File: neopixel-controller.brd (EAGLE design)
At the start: 23.8 x 26.7 mm, 12 parts, among them J1 Power, U1 ATTiny85

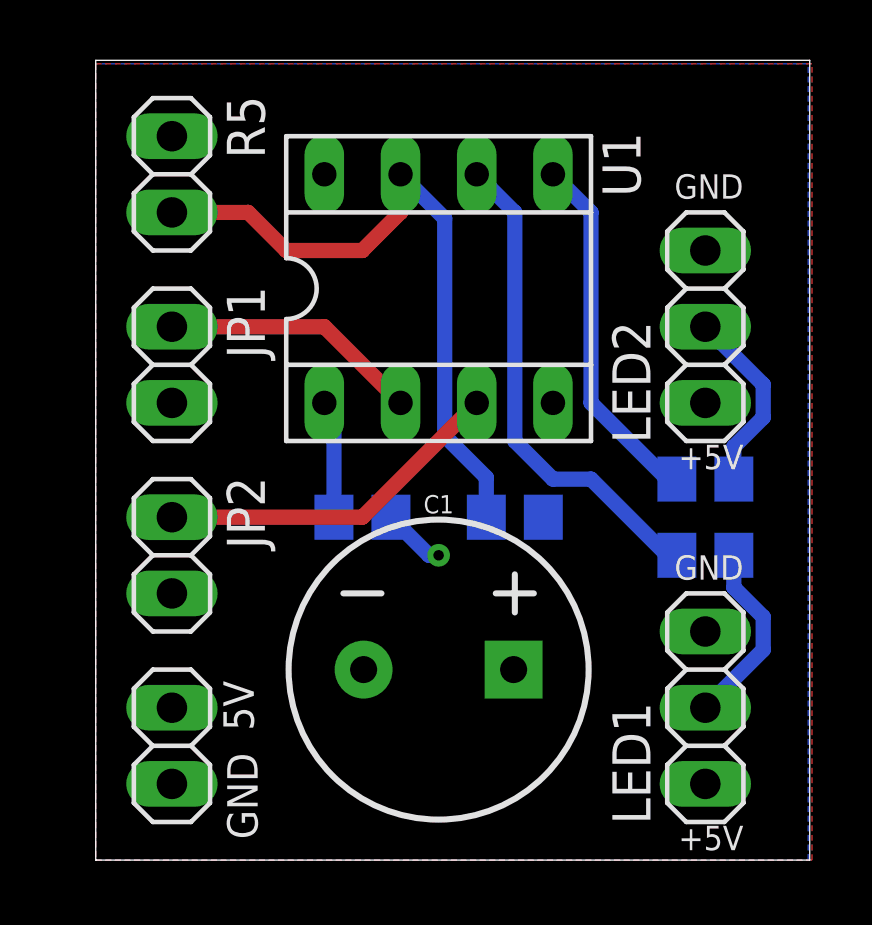
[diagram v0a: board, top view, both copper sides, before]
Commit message: Switch to both planes being ground planes
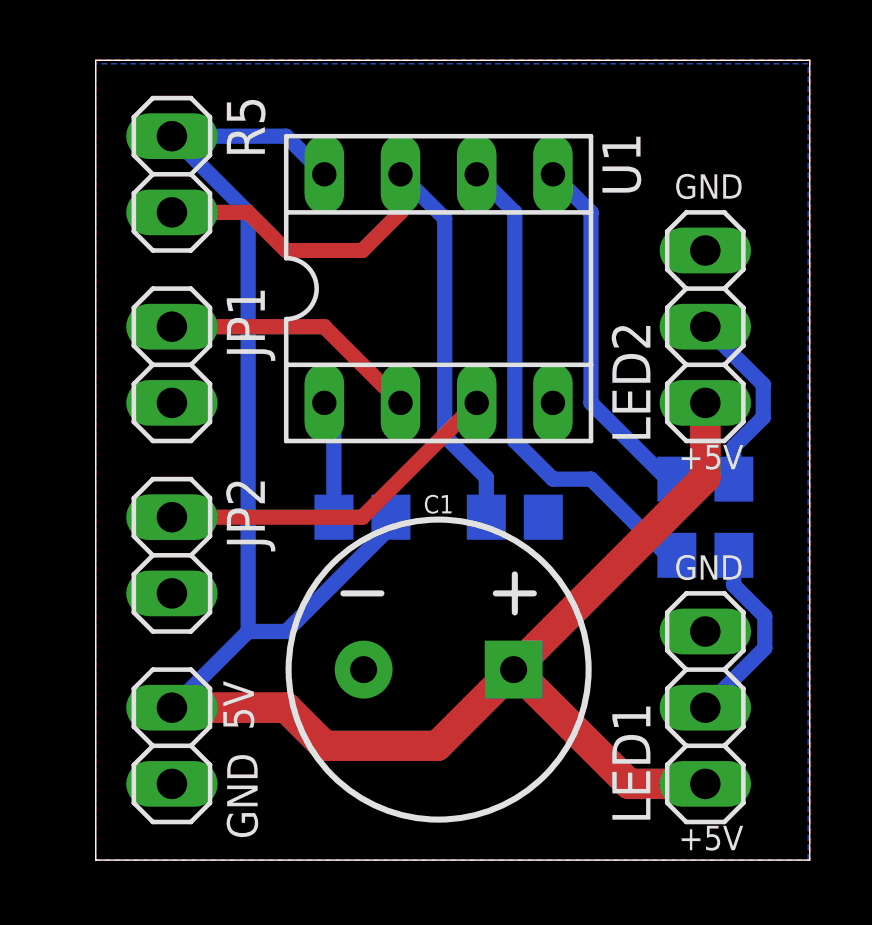
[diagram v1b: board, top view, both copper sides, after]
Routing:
- net VCC: track 2.12 -> 65.9 mm, vias 1 -> 0
- added copper zone on layer 1, net GND
- removed copper zone on layer 1, net VCC
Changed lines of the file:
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@@
 <?xml version="1.0" encoding="utf-8"?>
 <!DOCTYPE eagle SYSTEM "eagle.dtd">
-<eagle version="9.1.0">
+<eagle version="9.2.2">
 <drawing>
 <settings>
-<setting alwaysvectorfont="no"/>
+<setting alwaysvectorfont="yes"/>
 <setting verticaltext="up"/>
 </settings>
@@
 <classes>
 <class number="0" name="default" width="0" drill="0">
+<clearance class="0" value="0.205"/>
 </class>
 </classes>
@@
 </autorouter>
 <elements>
-<element name="C1" library="SparkFun-Capacitors" package="CPOL-RADIAL-5MM-10MM" value="1mF" x="11.43" y="6.35">
+<element name="C1" library="SparkFun-Capacitors" package="CPOL-RADIAL-5MM-10MM" value="1mF" x="11.43" y="6.35" smashed="yes">
+<attribute name="NAME" x="11.43" y="11.557" size="0.6096" layer="25" font="vector" ratio="20" align="bottom-center"/>
 <attribute name="PROD_ID" value="CAP-09538" x="11.43" y="6.35" size="1.778" layer="27" display="off"/>
+<attribute name="VALUE" x="11.43" y="1.143" size="0.6096" layer="27" font="vector" ratio="20" align="top-center"/>
 </element>
 <element name="J1" library="pinhead" library_urn="urn:adsk.eagle:library:325" package="1X02" package3d_urn="urn:adsk.eagle:package:22435/2" value="Power" x="2.54" y="3.81" smashed="yes" rot="R270">
@@
 <attribute name="VALUE" x="8.382" y="18.542" size="1.27" layer="27" ratio="10"/>
 </element>
-<element name="LED1" library="JoshCustom" package="NEOPIXEL_PINHEAD" value="Neopixel" x="20.32" y="5.08" rot="R90"/>
-<element name="LED2" library="JoshCustom" package="NEOPIXEL_PINHEAD" value="Neopixel" x="20.32" y="17.78" rot="R90"/>
+<element name="LED1" library="JoshCustom" package="NEOPIXEL_PINHEAD" value="Neopixel" x="20.32" y="5.08" smashed="yes" rot="R90">
+<attribute name="NAME" x="18.4912" y="1.1938" size="1.27" layer="25" font="vector" rot="R90"/>
+<attribute name="VALUE" x="23.495" y="1.27" size="1.27" layer="27" font="vector" rot="R90"/>
+</element>
+<element name="LED2" library="JoshCustom" package="NEOPIXEL_PINHEAD" value="Neopixel" x="20.32" y="17.78" smashed="yes" rot="R90">
+<attribute name="NAME" x="18.4912" y="13.8938" size="1.27" layer="25" font="vector" rot="R90"/>
+<attribute name="VALUE" x="23.495" y="13.97" size="1.27" layer="27" font="vector" rot="R90"/>
+</element>
 </elements>
 <signals>
@@
 <contactref element="R4" pad="2"/>
 <contactref element="R5" pad="1"/>
-<polygon width="0.1524" layer="1" thermals="no">
-<vertex x="0" y="0"/>
-<vertex x="23.876" y="0"/>
-<vertex x="23.876" y="26.543"/>
-<vertex x="0" y="26.543"/>
-</polygon>
-<wire x1="9.84" y1="11.43" x2="11.11" y2="10.16" width="0.508" layer="16"/>
-<wire x1="11.11" y1="10.16" x2="11.43" y2="10.16" width="0.508" layer="16"/>
-<via x="11.43" y="10.16" extent="1-16" drill="0.35"/>
+<wire x1="2.54" y1="24.13" x2="5.08" y2="21.59" width="0.508" layer="16"/>
+<wire x1="5.08" y1="21.59" x2="5.08" y2="7.62" width="0.508" layer="16"/>
+<wire x1="5.08" y1="7.62" x2="2.54" y2="5.08" width="0.508" layer="16"/>
+<wire x1="2.54" y1="24.13" x2="6.35" y2="24.13" width="0.508" layer="16"/>
+<wire x1="6.35" y1="24.13" x2="7.62" y2="22.86" width="0.508" layer="16"/>
+<wire x1="5.08" y1="7.62" x2="6.35" y2="7.62" width="0.508" layer="16"/>
+<wire x1="6.35" y1="7.62" x2="10.16" y2="11.43" width="0.508" layer="16"/>
+<wire x1="2.54" y1="5.08" x2="6.35" y2="5.08" width="1.016" layer="1"/>
+<wire x1="6.35" y1="5.08" x2="7.62" y2="3.81" width="1.016" layer="1"/>
+<wire x1="7.62" y1="3.81" x2="11.39" y2="3.81" width="1.016" layer="1"/>
+<wire x1="11.39" y1="3.81" x2="13.93" y2="6.35" width="1.016" layer="1"/>
+<wire x1="13.93" y1="6.35" x2="20.32" y2="12.74" width="1.016" layer="1"/>
+<wire x1="20.32" y1="12.74" x2="20.32" y2="15.24" width="1.016" layer="1"/>
+<wire x1="13.93" y1="6.35" x2="13.97" y2="6.35" width="1.016" layer="1"/>
+<wire x1="17.78" y1="2.54" x2="20.32" y2="2.54" width="1.016" layer="1"/>
+<wire x1="13.97" y1="6.35" x2="17.78" y2="2.54" width="1.016" layer="1"/>
+<wire x1="10.16" y1="11.43" x2="9.84" y2="11.43" width="0" layer="19" extent="16-16"/>
 </signal>
 <signal name="GND">
@@
 <vertex x="0" y="26.543"/>
 </polygon>
+<polygon width="0.3048" layer="1">
+<vertex x="0" y="0"/>
+<vertex x="0" y="26.67"/>
+<vertex x="23.8125" y="26.67"/>
+<vertex x="23.8125" y="0"/>
+</polygon>
 </signal>
 <signal name="N$5">
@@
 <contactref element="LED1" pad="2"/>
 <contactref element="R2" pad="2"/>
-<wire x1="21.27" y1="9.08436875" x2="21.27" y2="10.16" width="0.508" layer="16"/>
-<wire x1="22.2504" y1="8.10396875" x2="21.27" y2="9.08436875" width="0.508" layer="16"/>
-<wire x1="22.2504" y1="7.0104" x2="22.2504" y2="8.10396875" width="0.508" layer="16"/>
-<wire x1="20.32" y1="5.08" x2="22.2504" y2="7.0104" width="0.508" layer="16"/>
+<wire x1="21.27" y1="9.15875625" x2="21.27" y2="10.16" width="0.508" layer="16"/>
+<wire x1="22.303" y1="8.12575625" x2="21.27" y2="9.15875625" width="0.508" layer="16"/>
+<wire x1="22.303" y1="7.063" x2="22.303" y2="8.12575625" width="0.508" layer="16"/>
+<wire x1="20.32" y1="5.08" x2="22.303" y2="7.063" width="0.508" layer="16"/>
 </signal>
 <signal name="PB3">
@@
 </note>
 <note version="8.3" severity="warning">
+Since Version 8.3, EAGLE supports Fusion synchronisation.
+This feature will not be available in this version and saving
+the document will break the link to the Fusion PCB feature.
+</note>
+<note version="8.3" severity="warning">

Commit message: Final revision
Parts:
- added C2: 0.1uF, resistor:C0805
- C1: value 1mF -> 1000uF; device SparkFun-Capacitors:CPOL-RADIAL-5MM-10MM -> JoshCustom:CAP-3,5-8
- moved C1 1.62 mm to (11.7, 4.76)
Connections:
- net GND: now also C1.NEGATIVE, C2.2; no longer C1.-
- net VCC: now also C1.POSITIVE, C2.1; no longer C1.+
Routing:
- net VCC: track 65.9 -> 73.6 mm

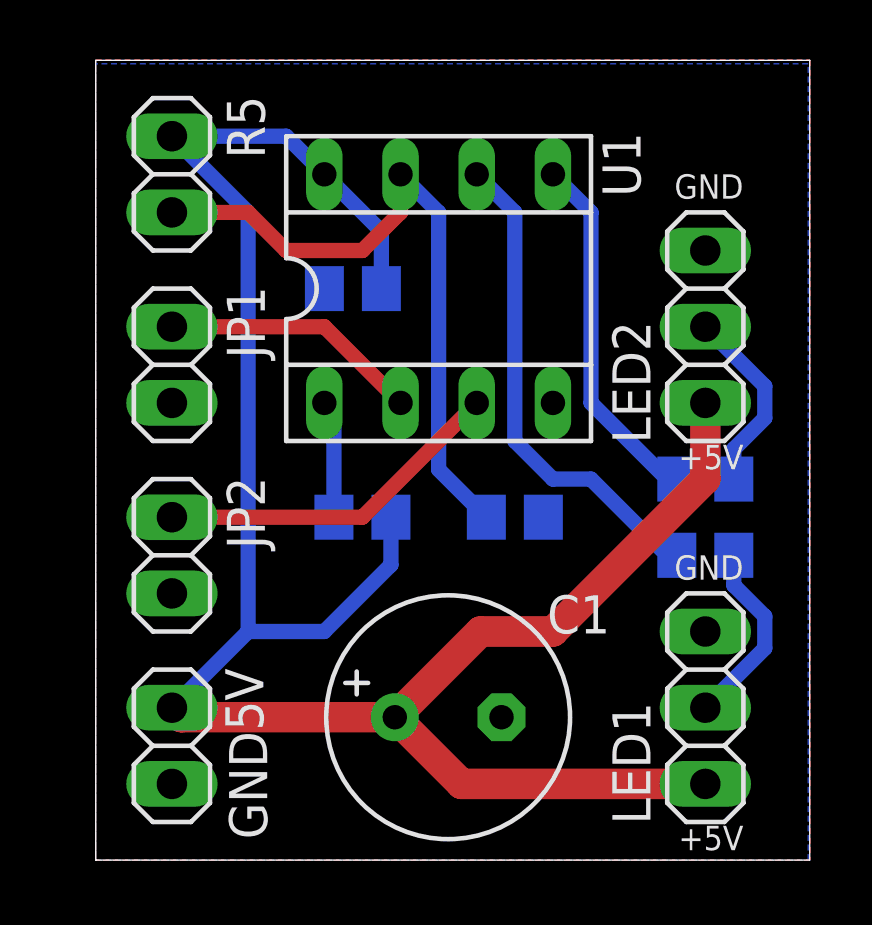
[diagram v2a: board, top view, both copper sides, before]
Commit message: Initial swap of Neopixel controller to SOIC ATTiny85
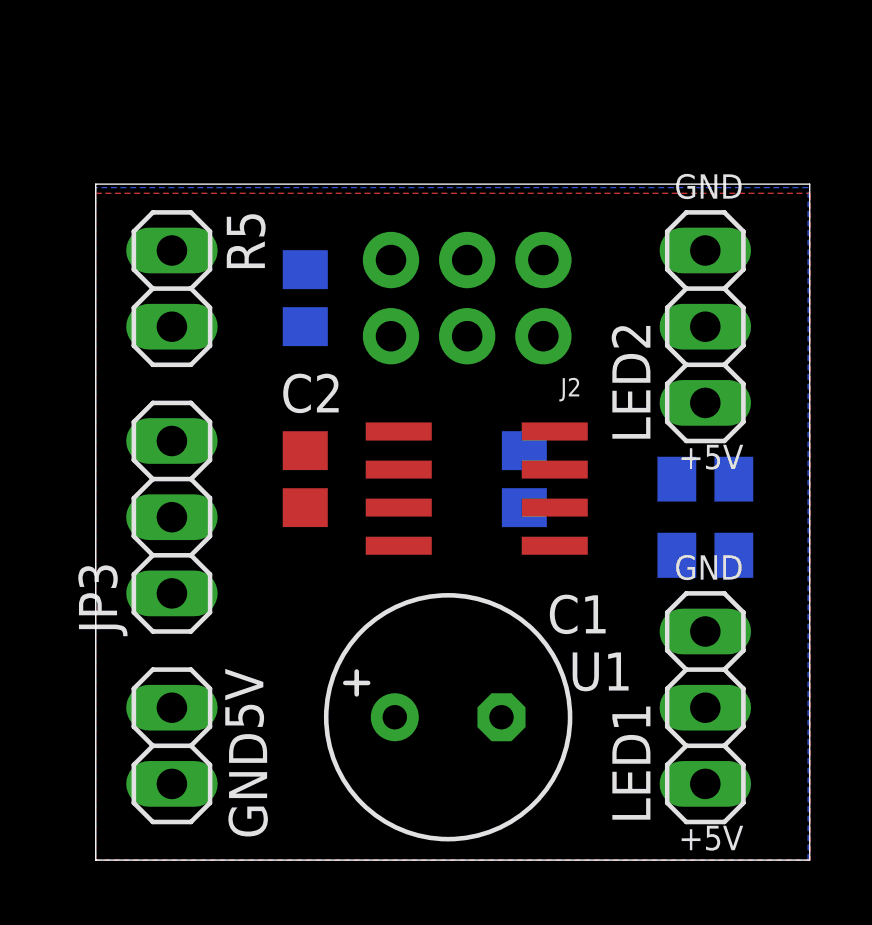
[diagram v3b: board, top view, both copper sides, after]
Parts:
- removed JP1, JP2: (no value), pinhead:1X02
- added J2: AVR_SPI_PROG_3X2NS, SparkFun-Connectors:2X3-NS
- added JP3: (no value), pinhead:1X03
- U1: device JoshCustom:SOCKET-08 -> JoshCustom:SOIC8
- moved R1 10.1 mm to (6.99, 18.7), turned to 90 degrees
- moved U1 6.79 mm to (12.7, 12.4), turned to 270 degrees
- moved C2 6.55 mm to (6.99, 12.7), flipped to the top, turned to 270 degrees
- moved R4 5.54 mm to (14.3, 12.7), turned to 270 degrees
- moved R5 3.81 mm to (2.54, 19.1)
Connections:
- removed net N$5: R4.1, U1.1
- new net RESET: J2.5, R4.1, U1.1
- net GND: now also J2.6, JP3.2; no longer JP1.2, JP2.2
- net LED1: now also J2.1
- net LED2: now also J2.4
- net PB2: now also J2.3
- net PB3: now also JP3.3; no longer JP1.1
- net PB4: now also JP3.1; no longer JP2.1
- net VCC: now also J2.2
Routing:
- net VCC: track 73.6 -> 0.00 mm
- net PB2: track 22.6 -> 0.00 mm
- net LED1: track 16.7 -> 0.00 mm
- net LED2: track 12.1 -> 0.00 mm
- net PB4: track 11.7 -> 0.00 mm
- net PB3: track 8.67 -> 0.00 mm
- net N$1: track 6.33 -> 0.00 mm
- net N$2: track 6.33 -> 0.00 mm
- net N$5: track 3.94 -> 0.00 mm
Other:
- board size 23.8 x 26.7 mm -> 23.8 x 22.5 mm

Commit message: Initial redesign for production run 2
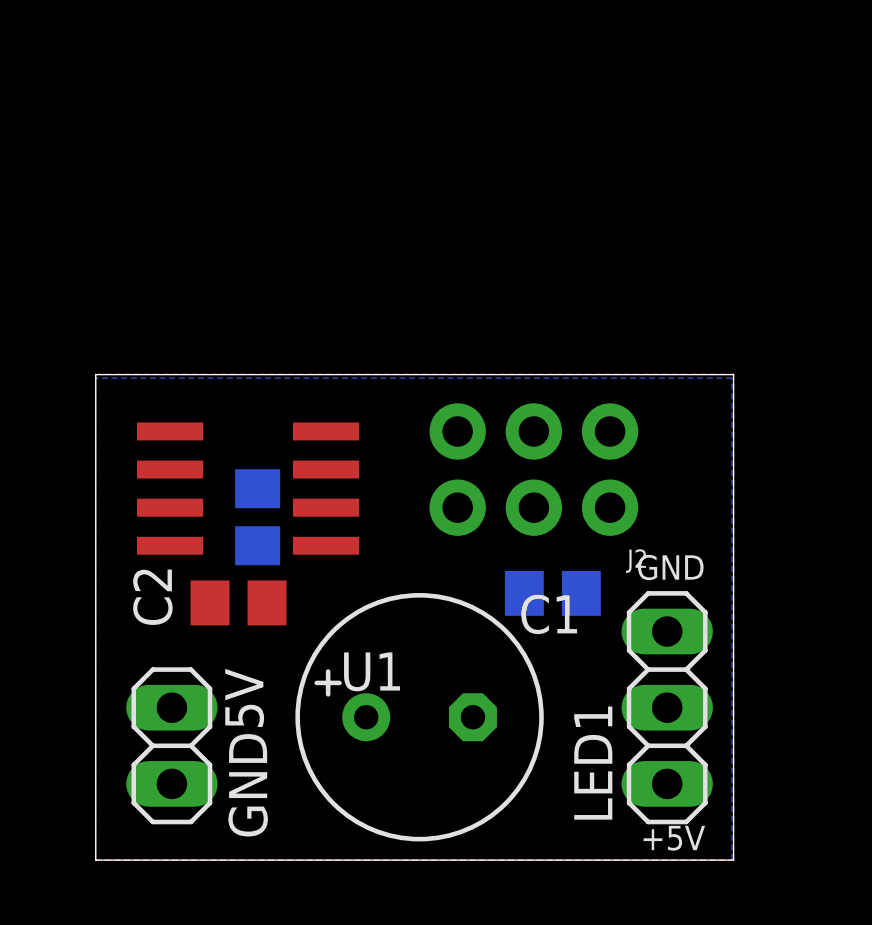
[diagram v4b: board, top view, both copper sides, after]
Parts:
- removed JP3: (no value), pinhead:1X03
- removed LED2: Neopixel, JoshCustom:NEOPIXEL_PINHEAD
- removed R1: 10k, resistor:R0805
- removed R3: 470, resistor:R0805
- removed R5: (no value), pinhead:1X02
- moved R4 8.98 mm to (5.40, 11.4)
- moved U1 7.62 mm to (5.08, 12.4)
- moved J2 6.13 mm to (14.6, 13.0)
- moved R2 5.24 mm to (15.2, 8.89)
- moved C2 4.69 mm to (4.76, 8.57), turned to 0 degrees
- moved LED1 1.27 mm to (19.1, 5.08)
- moved C1 0.95 mm to (10.8, 4.76)
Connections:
- removed net N$1: LED2.2, R3.2
- net GND: no longer JP3.2, LED2.3, R1.1
- net LED2: no longer R3.1
- net PB2: no longer R1.2, R5.2
- net PB3: no longer JP3.3
- net PB4: no longer JP3.1
- net VCC: no longer LED2.1, R5.1
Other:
- board size 23.8 x 22.5 mm -> 21.3 x 16.2 mm

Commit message: Revert neopixel-controller to neopixel-v1.0 and remove unnecessary things for 20th anniversary trophy production
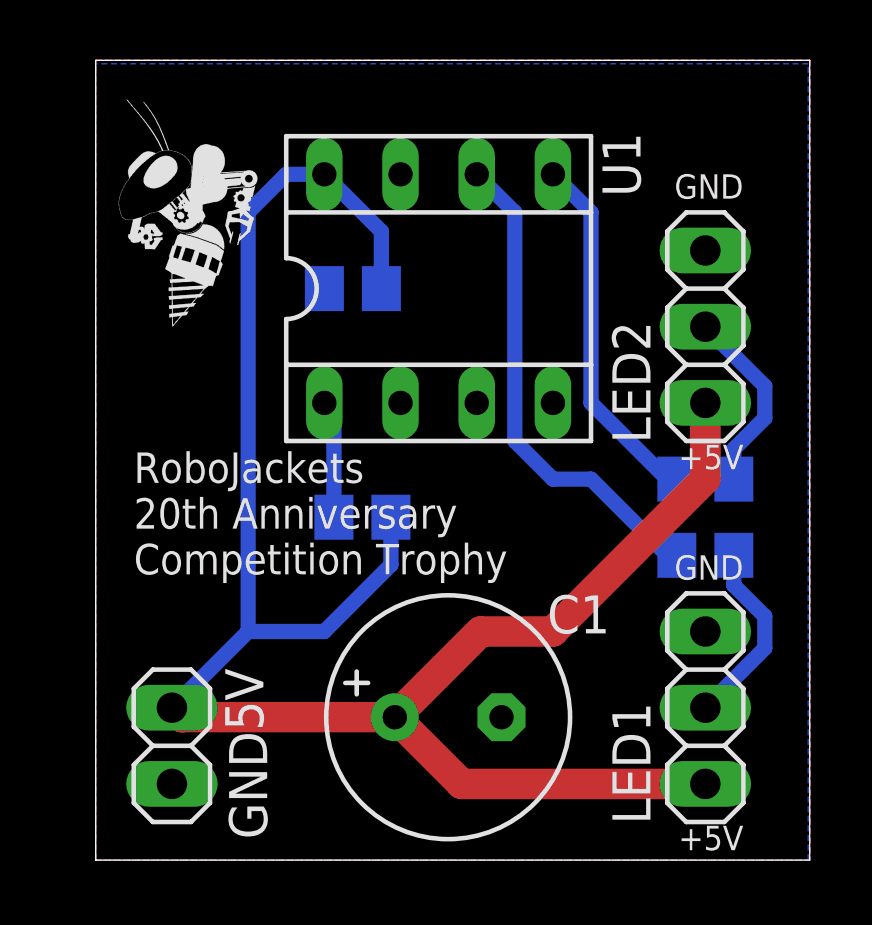
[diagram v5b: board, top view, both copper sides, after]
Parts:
- removed J2: AVR_SPI_PROG_3X2NS, SparkFun-Connectors:2X3-NS
- added LED2: Neopixel, JoshCustom:NEOPIXEL_PINHEAD
- added R3: 470, resistor:R0805
- added U$1: (no value), RoboJackets-Aesthetics:ROBOBUZZ_0.4X
- U1: device JoshCustom:SOIC8 -> JoshCustom:SOCKET-08
- moved C2 11.1 mm to (8.57, 19.1), flipped to the bottom
- moved U1 9.21 mm to (11.4, 19.1), turned to 0 degrees
- moved R2 5.24 mm to (20.3, 10.2)
- moved R4 3.49 mm to (8.89, 11.4), turned to 180 degrees
- moved LED1 1.27 mm to (20.3, 5.08)
- moved C1 0.95 mm to (11.7, 4.76)
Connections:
- removed net PB2: J2.3, U1.7
- removed net PB3: U1.2
- removed net PB4: U1.3
- removed net RESET: J2.5, R4.1, U1.1
- new net N$1: LED2.2, R3.2
- new net N$5: R4.1, U1.1
- net GND: now also LED2.3; no longer J2.6
- net LED1: no longer J2.1
- net LED2: now also R3.1; no longer J2.4
- net VCC: now also LED2.1; no longer J2.2
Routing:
- net VCC: track 0.00 -> 67.5 mm
- net LED1: track 0.00 -> 16.7 mm
- net LED2: track 0.00 -> 12.1 mm
- net N$1: track 0.00 -> 6.33 mm
- net N$2: track 0.00 -> 6.33 mm
- net N$5: track 0.00 -> 3.94 mm
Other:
- board size 21.3 x 16.2 mm -> 23.8 x 26.7 mm
- board text added: "ATtiny85"
- board text added: "RoboJackets 20th Anniversary Competition Trophy"
- board text added: "v1.1, Feb. 2019"
- board text removed: "ATTiny85"
- board text removed: "Josh Oldenburg Neopixel Controller v1.0, Dec. 2018"
